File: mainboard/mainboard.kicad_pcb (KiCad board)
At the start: 2 copper layers, 50 x 99.1 mm, 93 parts, among them J1 Eurorack_Power, J2 Inv1, J3 Inv2, J4 Ver2, J5 Ver1, J6 Conn_02x04_Counter_Clockwise, J7 Conn_02x03_Counter_Clockwise, J8 Out2, J9 Out1, Q1 BC557, Q10 BC557, Q11 BC557, Q12 BC557, Q13 BC547, Q14 BC547, Q15 BC557, Q16 BC557, Q17 BC547, Q18 BC547, Q19 BC557, Q2 BC557, Q20 BC557, Q21 BC547, Q22 BC547, Q23 BC557, Q24 BC547, Q25 BC547, Q3 BC547, Q4 BC547, Q5 BC547, Q6 BC547, Q7 BC547, Q8 BC547, Q9 BC557, U1 L78L09_TO92, U2 TL074

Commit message: Routing
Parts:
- moved Q14 87.4 mm to (16.8, 44.0)
- moved R9 84.8 mm to (52.9, 82.7), turned to -90 degrees
- moved R10 84.5 mm to (52.9, 33.1), turned to -90 degrees
- moved R30 79.0 mm to (21.1, 43.8), turned to 0 degrees
- moved R28 78.9 mm to (21.1, 41.5), turned to 0 degrees
- moved Q10 78.9 mm to (40.1, 50.8), turned to -90 degrees
- moved R44 76.7 mm to (24.8, 61.5)
- moved R20 76.4 mm to (46.7, 57.8), turned to 90 degrees
- moved R26 76.4 mm to (44.2, 57.8), turned to 90 degrees
- moved R16 75.5 mm to (41.3, 47.5), turned to 0 degrees
- moved Q2 75.0 mm to (56.2, 58.5), turned to 90 degrees
- moved Q8 74.9 mm to (55.4, 44.5)
- moved Q1 74.8 mm to (56.3, 108.3), turned to 90 degrees
- moved Q6 74.8 mm to (60.6, 44.5)
- moved Q5 74.7 mm to (60.6, 94.5)
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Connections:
- U2 pad 1: MIDO1 -> Net-(R34-Pad2)
- U2 pad 10: Net-(C4-Pad1) -> Net-(R15-Pad2)
- U2 pad 12: Net-(R15-Pad2) -> Net-(C4-Pad1)
- U2 pad 13: MIDO2 -> Net-(R33-Pad2)
- U2 pad 14: MIDO2 -> Net-(R33-Pad2)
- U2 pad 2: MIDO1 -> Net-(R34-Pad2)
- U2 pad 3: Net-(R13-Pad2) -> Out1
- U2 pad 5: Out1 -> Net-(R13-Pad2)
- U2 pad 6: Net-(R34-Pad2) -> MIDO1
- U2 pad 7: Net-(R34-Pad2) -> MIDO1
- U2 pad 8: Net-(R33-Pad2) -> MIDO2
- U2 pad 9: Net-(R33-Pad2) -> MIDO2
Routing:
- net GND: track 0.00 -> 340.3 mm, vias 0 -> 1
- net +9V: track 0.00 -> 281.1 mm
- net Net-(Q11-Pad2): track 0.00 -> 86.9 mm
- net Net-(Q10-Pad1): track 0.00 -> 65.7 mm
- net Out1: track 0.00 -> 56.9 mm, vias 0 -> 1
- net MIDO2: track 0.00 -> 54.4 mm
- net MIDO1: track 0.00 -> 38.8 mm
- net Net-(R33-Pad2): track 0.00 -> 33.9 mm
- net Net-(C8-Pad1): track 0.00 -> 29.4 mm
- net Net-(Q7-Pad2): track 0.00 -> 27.2 mm
- net Net-(Q8-Pad2): track 0.00 -> 26.7 mm
- net Net-(C4-Pad1): track 0.00 -> 25.8 mm
- net N3: track 0.00 -> 25.7 mm
- net N1: track 0.00 -> 25.3 mm
- net Net-(R1-Pad1): track 0.00 -> 24.8 mm, vias 0 -> 1
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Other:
- board text added: "panel components other side"
- board text added: "panel components this side"
- board text added: "pcb by Neil Massey from a circuit by Ciat-Lonbarde thanks to Josh Rodriguez"

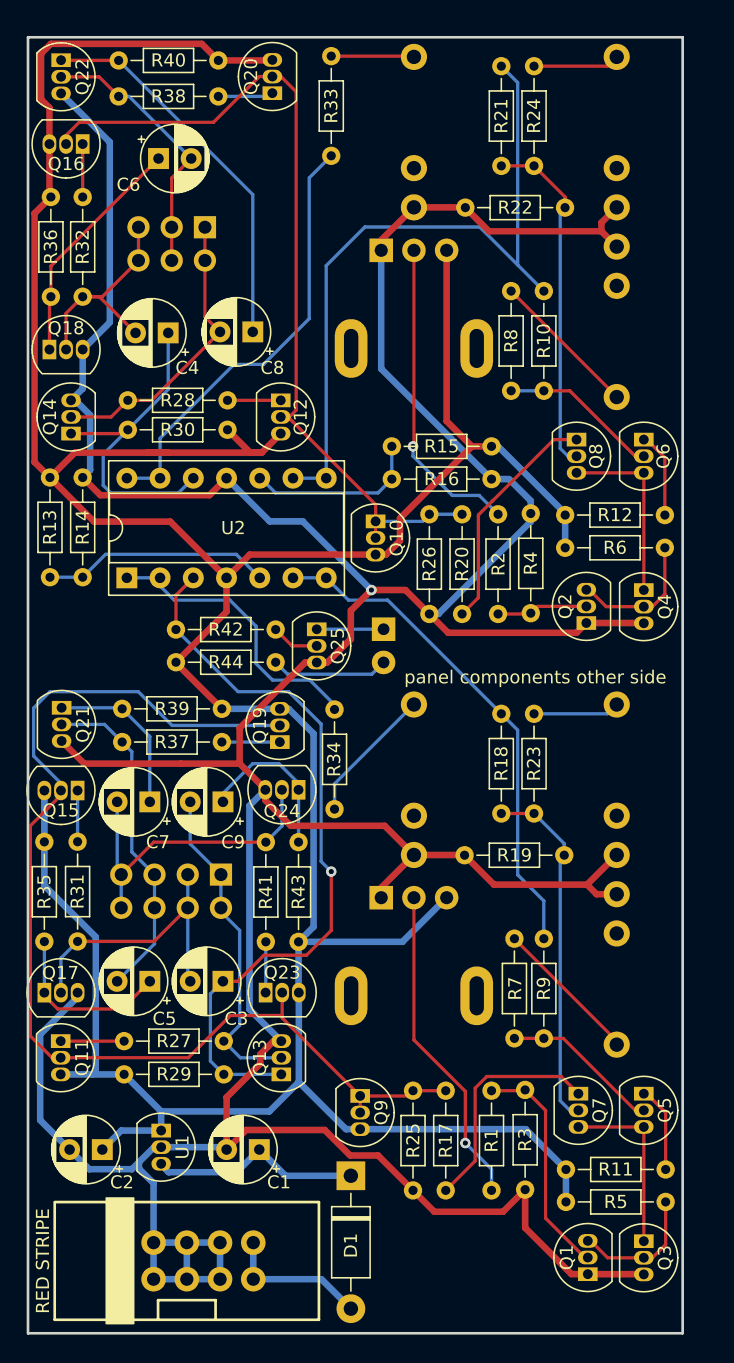
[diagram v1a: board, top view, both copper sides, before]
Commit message: Attenuator version
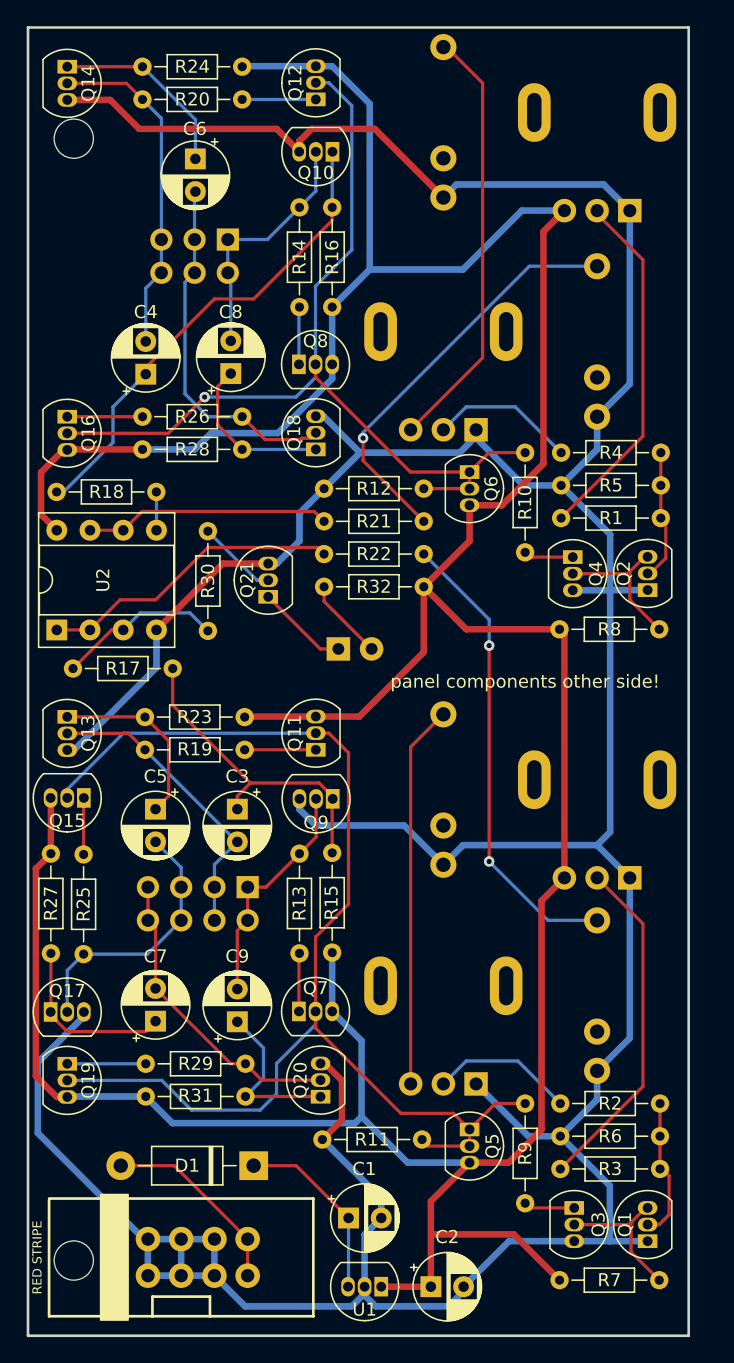
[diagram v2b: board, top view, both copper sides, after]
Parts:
- removed J8: Out2, winterbloom:AudioJack_WQP518MA
- removed J9: Out1, winterbloom:AudioJack_WQP518MA
- removed Q22, Q24, Q25: BC547, Package_TO_SOT_THT:TO-92_Inline
- removed Q23: BC557, Package_TO_SOT_THT:TO-92_Inline
- removed R33, R34: 10k, Resistor_THT:R_Axial_DIN0204_L3.6mm_D1.6mm_P7.62mm_Horizontal
- removed R35, R36, R37, R38, R39, R40, R41, R43, R44: 4.7k, Resistor_THT:R_Axial_DIN0204_L3.6mm_D1.6mm_P7.62mm_Horizontal
- removed R42: 100k, Resistor_THT:R_Axial_DIN0204_L3.6mm_D1.6mm_P7.62mm_Horizontal
- added RV3: Rate1, winterbloom:Potentiometer_Alpha_R0904N, B.Cu at (57.0, 70.5)
- added RV4: CV2, winterbloom:Potentiometer_Alpha_R0904N, B.Cu at (45.2, 36.2)
- J2: value Inv1 -> CV1
- J3: value Inv2 -> CV2
- J4: value Ver2 -> Conn_02x04_Counter_Clockwise; footprint winterbloom:AudioJack_WQP518MA -> Connector_PinSocket_2.54mm:PinSocket_2x04_P2.54mm_Vertical
- J5: value Ver1 -> Conn_02x03_Counter_Clockwise; footprint winterbloom:AudioJack_WQP518MA -> Connector_PinSocket_2.54mm:PinSocket_2x03_P2.54mm_Vertical
- J6: value Conn_02x04_Counter_Clockwise -> Out2; footprint Connector_PinSocket_2.54mm:PinSocket_2x04_P2.54mm_Vertical -> winterbloom:AudioJack_WQP518MA
- J7: value Conn_02x03_Counter_Clockwise -> Out1; footprint Connector_PinSocket_2.54mm:PinSocket_2x03_P2.54mm_Vertical -> winterbloom:AudioJack_WQP518MA
- Q10, Q20, Q9: value BC557 -> BC547
- Q5, Q6, Q7, Q8: value BC547 -> BC557
- R1: value 470k -> 220k
- R10, R9: value 10k -> 4.7k
- R11, R12: value 4.7k -> 2.2M
- R13, R14, R15, R16: value 22k -> 4.7k
- R17: value 4.7k -> 10k
- R19, R25, R26: value 2.2M -> 4.7k
- R22: value 2.2M -> 10k
- R23, R24: value 100k -> 4.7k
- R3: value 4.7k -> 220k
- R30: value 4.7k -> 100k
- R4: value 4.7k -> 470k
- R5, R6: value 470k -> 2.2k
- R7, R8: value 100k -> 470k
- RV1: value Rate1 -> Rate2
- RV2: value Rate2 -> CV1
- U2: value TL074 -> TL072; footprint Package_DIP:DIP-14_W7.62mm_Socket -> Package_DIP:DIP-8_W7.62mm_Socket
- moved Q20 76.8 mm to (35.9, 94.7)
- moved RV1 69.0 mm to (57.0, 19.5), turned to 180 degrees
- moved J7 65.3 mm to (57.0, 86.2), turned to 180 degrees
- moved J4 64.9 mm to (30.3, 78.7), turned to 90 degrees
- moved R5 55.3 mm to (54.2, 48.0), turned to 0 degrees
- moved R1 51.7 mm to (54.2, 50.5), turned to 0 degrees
- moved J6 50.5 mm to (57.0, 36.2), turned to 180 degrees
- moved J5 50.3 mm to (28.8, 29.2), turned to 90 degrees
- moved R17 49.0 mm to (16.9, 62.0), turned to 0 degrees
- moved RV2 48.8 mm to (45.2, 86.2), turned to 180 degrees
- moved R20 46.3 mm to (22.2, 18.5), turned to 0 degrees
- moved R6 45.7 mm to (54.2, 97.8), turned to 0 degrees
- moved R2 45.3 mm to (54.2, 95.2), turned to 0 degrees
- moved R21 35.3 mm to (43.8, 50.8), turned to 180 degrees
- moved R13 34.5 mm to (34.2, 76.2)
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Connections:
- C3 pad 1: Out1 -> Net-(C3-Pad1)
- Q10 pad 1: Net-(Q10-Pad1) -> Net-(C4-Pad1)
- Q10 pad 2: Net-(Q10-Pad1) -> N5
- Q10 pad 3: +9V -> GND
- Q12 pad 2: Net-(Q10-Pad1) -> Net-(Q12-Pad2)
- Q13 pad 1: Out1 -> Net-(C5-Pad1)
- Q13 pad 2: N1 -> N2
- Q14 pad 1: Net-(C4-Pad1) -> Net-(C6-Pad1)
- Q14 pad 2: N5 -> N6
- Q16 pad 2: Net-(Q10-Pad1) -> Net-(Q12-Pad2)
- Q17 pad 1: Net-(C5-Pad1) -> Net-(C7-Pad1)
- Q17 pad 2: N2 -> N3
- Q18 pad 1: Net-(C6-Pad1) -> Net-(C8-Pad1)
- Q18 pad 2: N6 -> N7
- Q20 pad 1: Net-(Q20-Pad1) -> Net-(C9-Pad1)
- Q20 pad 2: Net-(Q10-Pad1) -> N4
- Q20 pad 3: +9V -> GND
- Q21 pad 1: Net-(C7-Pad1) -> Net-(D2-Pad1)
- Q21 pad 2: N3 -> Net-(Q21-Pad2)
- Q5 pad 1: Net-(Q5-Pad1) -> Net-(Q11-Pad2)
- Q5 pad 2: Net-(Q5-Pad2) -> Net-(Q11-Pad2)
- Q5 pad 3: Net-(Q3-Pad1) -> +9V
- Q6 pad 1: Net-(Q6-Pad1) -> Net-(Q12-Pad2)
- Q6 pad 2: Net-(Q6-Pad2) -> Net-(Q12-Pad2)
- Q6 pad 3: Net-(Q4-Pad1) -> +9V
- Q7 pad 2: Net-(Q7-Pad2) -> Net-(Q11-Pad2)
- Q7 pad 3: Net-(Q3-Pad1) -> +9V
- Q8 pad 2: Net-(Q8-Pad2) -> Net-(Q12-Pad2)
- Q8 pad 3: Net-(Q4-Pad1) -> +9V
- Q9 pad 1: Net-(Q11-Pad2) -> Net-(C3-Pad1)
- Q9 pad 2: Net-(Q11-Pad2) -> N1
- Q9 pad 3: +9V -> GND
- R1 pad 2: Net-(Q1-Pad2) -> Net-(Q2-Pad2)
- R10 pad 1: MIDO2 -> Net-(Q4-Pad1)
- R10 pad 2: Net-(Q6-Pad2) -> Net-(Q12-Pad2)
- R11 pad 1: +9V -> GND
- R11 pad 2: Net-(Q5-Pad1) -> Net-(Q11-Pad2)
- R12 pad 1: +9V -> GND
- R12 pad 2: Net-(Q6-Pad1) -> Net-(Q12-Pad2)
- R13 pad 1: +9V -> N1
- R13 pad 2: Net-(R13-Pad2) -> Net-(Q7-Pad1)
- R14 pad 1: Net-(R13-Pad2) -> N5
- R14 pad 2: GND -> Net-(Q8-Pad1)
- R15 pad 1: +9V -> Net-(C3-Pad1)
- R15 pad 2: Net-(R15-Pad2) -> +9V
- R16 pad 1: Net-(R15-Pad2) -> Net-(C4-Pad1)
- R16 pad 2: GND -> +9V
- R17 pad 1: Net-(Q7-Pad1) -> Out1
- R17 pad 2: Net-(Q11-Pad2) -> Net-(C3-Pad1)
- R18 pad 1: MIDO1 -> Net-(R18-Pad1)
- R18 pad 2: Net-(Q7-Pad2) -> Net-(C4-Pad1)
- R19 pad 1: GND -> N2
- R19 pad 2: Net-(Q7-Pad2) -> Net-(Q11-Pad1)
- R2 pad 2: Net-(Q2-Pad2) -> Net-(Q1-Pad2)
- R20 pad 1: Net-(Q8-Pad1) -> N6
- R20 pad 2: Net-(Q10-Pad1) -> Net-(Q12-Pad1)
- R21 pad 1: MIDO2 -> Net-(J6-PadT)
- R21 pad 2: Net-(Q8-Pad2) -> Net-(R21-Pad2)
- R22 pad 1: GND -> Net-(J7-PadT)
- R22 pad 2: Net-(Q8-Pad2) -> Net-(R22-Pad2)
- R23 pad 1: Net-(J5-PadT) -> Net-(C5-Pad1)
- R23 pad 2: Net-(Q7-Pad2) -> +9V
- R24 pad 1: Net-(J4-PadT) -> Net-(C6-Pad1)
- R24 pad 2: Net-(Q8-Pad2) -> +9V
- R25 pad 1: GND -> N3
- R25 pad 2: Net-(Q11-Pad2) -> Net-(Q15-Pad1)
- R26 pad 1: GND -> N7
- R26 pad 2: Net-(Q10-Pad1) -> Net-(Q16-Pad1)
- R27 pad 1: N1 -> Net-(C7-Pad1)
- R27 pad 2: Net-(Q11-Pad1) -> +9V
- R28 pad 1: N5 -> Net-(C8-Pad1)
- R28 pad 2: Net-(Q12-Pad1) -> +9V
- R29 pad 1: Out1 -> N4
- R29 pad 2: +9V -> Net-(Q19-Pad1)
- R3 pad 1: GND -> Net-(R3-Pad1)
- R30 pad 1: Net-(C4-Pad1) -> Net-(Q21-Pad2)
- R30 pad 2: +9V -> Out1
- R31 pad 1: N2 -> Net-(C9-Pad1)
- R31 pad 2: Net-(Q15-Pad1) -> +9V
- R32 pad 1: N6 -> +9V
- R32 pad 2: Net-(Q16-Pad1) -> Net-(D2-Pad2)
- R4 pad 1: GND -> Net-(R4-Pad1)
- R5 pad 1: Net-(Q1-Pad3) -> GND
- R5 pad 2: +9V -> Net-(Q2-Pad2)
- R6 pad 1: Net-(Q2-Pad3) -> GND
- R6 pad 2: +9V -> Net-(Q1-Pad2)
- R7 pad 1: Net-(Q5-Pad2) -> Net-(Q1-Pad3)
- R7 pad 2: Net-(J2-PadT) -> +9V
- R8 pad 1: Net-(Q6-Pad2) -> Net-(Q2-Pad3)
- R8 pad 2: Net-(J3-PadT) -> +9V
- R9 pad 1: MIDO1 -> Net-(Q3-Pad1)
- R9 pad 2: Net-(Q5-Pad2) -> Net-(Q11-Pad2)
- RV2 pad 3: +9V -> Net-(J2-PadT)
- U2 pad 1: Net-(R34-Pad2) -> Net-(R22-Pad2)
- U2 pad 2: Net-(R34-Pad2) -> Net-(R22-Pad2)
- U2 pad 4: +9V -> GND
- U2 pad 5: Net-(R13-Pad2) -> Net-(R18-Pad1)
- U2 pad 6: MIDO1 -> Net-(R21-Pad2)
- U2 pad 7: MIDO1 -> Net-(R21-Pad2)
- U2 pad 8: MIDO2 -> +9V
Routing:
- net Net-(Q12-Pad2): track 0.00 -> 71.5 mm, vias 0 -> 1
- net Net-(Q10-Pad1): track 65.7 -> 0.00 mm
- net MIDO2: track 54.4 -> 0.00 mm
- net Out1: track 56.9 -> 12.6 mm, vias 1 -> 0
- net MIDO1: track 38.8 -> 0.00 mm
- net Net-(J7-PadT): track 0.00 -> 35.7 mm, vias 0 -> 2
- net Net-(R33-Pad2): track 33.9 -> 0.00 mm
- net Net-(J6-PadT): track 0.00 -> 31.9 mm, vias 0 -> 1
- net Net-(Q7-Pad2): track 27.2 -> 0.00 mm
- net Net-(Q8-Pad2): track 26.7 -> 0.00 mm
- net Net-(R3-Pad1): track 0.00 -> 26.3 mm
- net Net-(C3-Pad1): track 0.00 -> 24.7 mm
- net Net-(R22-Pad2): track 0.00 -> 23.2 mm
- net Net-(R34-Pad2): track 22.3 -> 0.00 mm
- net Net-(J3-PadT): track 11.4 -> 32.9 mm
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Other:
- board size 50 x 99.1 mm -> 50.5 x 100 mm
- board text added: "panel components other side!"
- board text added: "panel components this side!"
- board text added: "pcb: Neil Massey circuit: Ciat-Lonbarde thanks: Josh Rodriguez"
- board text removed: "panel components other side"
- board text removed: "panel components this side"
- board text removed: "pcb by Neil Massey from a circuit by Ciat-Lonbarde thanks to Josh Rodriguez"

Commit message: Front panel
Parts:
- added D3: BAT85, Diode_THT:D_DO-35_SOD27_P7.62mm_Horizontal, F.Cu at (54.0, 80.0)
- added D4: BAT85, Diode_THT:D_DO-35_SOD27_P7.62mm_Horizontal, F.Cu at (54.8, 29.6)
- moved RV2 12.1 mm to (57.2, 87.5)
- moved RV4 12.0 mm to (57.2, 37.0)
- moved J2 12.0 mm to (57.2, 70.0)
- moved J3 12.0 mm to (57.2, 19.5)
- moved J7 11.8 mm to (45.2, 87.5)
- moved J6 11.8 mm to (45.2, 37.0)
- moved RV3 11.8 mm to (45.2, 70.0)
- moved RV1 11.8 mm to (45.2, 19.5)
- moved D2 11.7 mm to (27.5, 54.0), turned to -90 degrees
- moved Q21 6.90 mm to (28.0, 50.8)
- moved R30 6.02 mm to (31.8, 47.5)
- moved Q2 3.50 mm to (60.9, 59.5)
- moved Q4 3.50 mm to (55.1, 57.0)
- moved R1 3.50 mm to (54.2, 54.0)
- moved R4 3.50 mm to (54.2, 49.0)
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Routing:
- net +9V: track 289.9 -> 243.0 mm
- net GND: track 334.8 -> 358.5 mm
- net Net-(J6-PadT): track 31.9 -> 23.3 mm
- net Net-(R2-Pad1): track 11.0 -> 4.21 mm
- net Out1: track 12.6 -> 18.1 mm
- net Net-(R4-Pad1): track 11.2 -> 5.74 mm
- net Net-(D2-Pad1): track 7.01 -> 3.41 mm
- net Net-(Q12-Pad2): track 71.5 -> 68.2 mm
- net Net-(R1-Pad1): track 27.5 -> 30.7 mm
- net Net-(J2-PadT): track 29.3 -> 32.1 mm
- net Net-(D2-Pad2): track 6.26 -> 8.96 mm
- net Net-(R3-Pad1): track 26.3 -> 29.0 mm
- net Net-(J3-PadT): track 32.9 -> 31.0 mm
- net Net-(Q21-Pad2): track 6.16 -> 4.59 mm
- net Net-(R22-Pad2): track 23.2 -> 24.0 mm
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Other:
- outline, holes or cut-outs redrawn

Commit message: Trace corrections, panel corrections
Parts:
- moved R30 0.25 mm to (31.8, 47.8)
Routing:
- net Net-(Q1-Pad2): track 10.6 -> 9.93 mm
